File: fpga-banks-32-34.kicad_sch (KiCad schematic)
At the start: 9 parts, among them U4 XC7K160T-FFG676

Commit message: Clean schematic DRC
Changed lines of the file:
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@@
     (pin "T6")
   )
-  (symbol (lib_id "sodimm-ddr5-tester:GND") (at 79.375 253.365 0) (mirror y) (unit 1)
+  (symbol (lib_id "power:GND") (at 79.375 253.365 0) (mirror y) (unit 1)
     (in_bom yes) (on_board yes) (fields_autoplaced)
     (property "Reference" "#PWR0280" (id 0) (at 79.375 259.715 0)
       (effects (font (size 1.27 1.27)) hide)
     )
-    (property "Value" "GND" (id 1) (at 79.375 257.81 0))
-    (property "Footprint" "" (id 2) (at 79.375 253.365 0)
-      (effects (font (size 1.27 1.27)) hide)
-    )
-    (property "Datasheet" "" (id 3) (at 79.375 253.365 0)
-      (effects (font (size 1.27 1.27)) hide)
+    (property "Value" "GND" (id 1) (at 70.485 258.445 0)
+      (effects (font (size 1.27 1.27) (thickness 0.15)) (justify left bottom))
+    )
+    (property "Footprint" "" (id 2) (at 70.485 260.985 0)
+      (effects (font (size 1.27 1.27) (thickness 0.15)) (justify left bottom) hide)
+    )
+    (property "Datasheet" "" (id 3) (at 70.485 266.065 0)
+      (effects (font (size 1.27 1.27) (thickness 0.15)) (justify left bottom) hide)
     )
     (property "Author" "Antmicro" (id 4) (at 70.485 260.985 0)
@@
     (pin "1")
   )
-  (symbol (lib_id "sodimm-ddr5-tester:GND") (at 72.39 253.365 0) (mirror y) (unit 1)
+  (symbol (lib_id "power:GND") (at 72.39 253.365 0) (mirror y) (unit 1)
     (in_bom yes) (on_board yes) (fields_autoplaced)
     (property "Reference" "#PWR0279" (id 0) (at 72.39 259.715 0)
       (effects (font (size 1.27 1.27)) hide)
     )
-    (property "Value" "GND" (id 1) (at 72.39 257.81 0))
-    (property "Footprint" "" (id 2) (at 72.39 253.365 0)
-      (effects (font (size 1.27 1.27)) hide)
-    )
-    (property "Datasheet" "" (id 3) (at 72.39 253.365 0)
-      (effects (font (size 1.27 1.27)) hide)
+    (property "Value" "GND" (id 1) (at 63.5 258.445 0)
+      (effects (font (size 1.27 1.27) (thickness 0.15)) (justify left bottom))
+    )
+    (property "Footprint" "" (id 2) (at 63.5 260.985 0)
+      (effects (font (size 1.27 1.27) (thickness 0.15)) (justify left bottom) hide)
+    )
+    (property "Datasheet" "" (id 3) (at 63.5 266.065 0)
+      (effects (font (size 1.27 1.27) (thickness 0.15)) (justify left bottom) hide)
     )
     (property "Author" "Antmicro" (id 4) (at 63.5 260.985 0)
@@
     (pin "2")
   )
-  (symbol (lib_id "sodimm-ddr5-tester:GND") (at 34.29 253.365 0) (mirror y) (unit 1)
+  (symbol (lib_id "power:GND") (at 34.29 253.365 0) (mirror y) (unit 1)
     (in_bom yes) (on_board yes) (fields_autoplaced)
     (property "Reference" "#PWR0277" (id 0) (at 34.29 259.715 0)
       (effects (font (size 1.27 1.27)) hide)
     )
-    (property "Value" "GND" (id 1) (at 34.29 257.81 0))
-    (property "Footprint" "" (id 2) (at 34.29 253.365 0)
-      (effects (font (size 1.27 1.27)) hide)
-    )
-    (property "Datasheet" "" (id 3) (at 34.29 253.365 0)
-      (effects (font (size 1.27 1.27)) hide)
+    (property "Value" "GND" (id 1) (at 25.4 258.445 0)
+      (effects (font (size 1.27 1.27) (thickness 0.15)) (justify left bottom))
+    )
+    (property "Footprint" "" (id 2) (at 25.4 260.985 0)
+      (effects (font (size 1.27 1.27) (thickness 0.15)) (justify left bottom) hide)
+    )
+    (property "Datasheet" "" (id 3) (at 25.4 266.065 0)
+      (effects (font (size 1.27 1.27) (thickness 0.15)) (justify left bottom) hide)
     )
     (property "Author" "Antmicro" (id 4) (at 25.4 260.985 0)
@@
     (pin "1")
   )
-  (symbol (lib_id "sodimm-ddr5-tester:GND") (at 140.335 255.905 0) (mirror y) (unit 1)
+  (symbol (lib_id "power:GND") (at 140.335 255.905 0) (mirror y) (unit 1)
     (in_bom yes) (on_board yes) (fields_autoplaced)
     (property "Reference" "#PWR0281" (id 0) (at 140.335 262.255 0)
       (effects (font (size 1.27 1.27)) hide)
     )
-    (property "Value" "GND" (id 1) (at 140.335 260.985 0))
-    (property "Footprint" "" (id 2) (at 140.335 255.905 0)
-      (effects (font (size 1.27 1.27)) hide)
-    )
-    (property "Datasheet" "" (id 3) (at 140.335 255.905 0)
-      (effects (font (size 1.27 1.27)) hide)
+    (property "Value" "GND" (id 1) (at 131.445 260.985 0)
+      (effects (font (size 1.27 1.27) (thickness 0.15)) (justify left bottom))
+    )
+    (property "Footprint" "" (id 2) (at 131.445 263.525 0)
+      (effects (font (size 1.27 1.27) (thickness 0.15)) (justify left bottom) hide)
+    )
+    (property "Datasheet" "" (id 3) (at 131.445 268.605 0)
+      (effects (font (size 1.27 1.27) (thickness 0.15)) (justify left bottom) hide)
     )
     (property "Author" "Antmicro" (id 4) (at 131.445 263.525 0)
@@
     (pin "1")
   )
-  (symbol (lib_id "sodimm-ddr5-tester:R_80R6_0402_EIA") (at 131.445 245.745 0) (unit 1)
+  (symbol (lib_name "R_80R6_0402_EIA_1") (lib_id "sodimm-ddr5-tester:R_80R6_0402_EIA") (at 131.445 245.745 0) (unit 1)
     (in_bom yes) (on_board yes) (fields_autoplaced)
     (property "Reference" "R133" (id 0) (at 133.985 240.03 0)
@@
     (pin "2")
   )
-  (symbol (lib_id "sodimm-ddr5-tester:+1V1") (at 142.24 243.84 0) (unit 1)
+  (symbol (lib_id "power:+1V1") (at 142.24 243.84 0) (unit 1)
     (in_bom yes) (on_board yes) (fields_autoplaced)
     (property "Reference" "#PWR0282" (id 0) (at 142.24 247.65 0)
       (effects (font (size 1.27 1.27)) hide)
     )
-    (property "Value" "+1V1" (id 1) (at 142.24 238.76 0))
+    (property "Value" "+1V1" (id 1) (at 142.24 240.284 0))
     (property "Footprint" "" (id 2) (at 142.24 243.84 0)
       (effects (font (size 1.27 1.27)) hide)
@@
     (pin "2")
   )
-  (symbol (lib_id "sodimm-ddr5-tester:+1V1") (at 34.29 236.855 0) (unit 1)
+  (symbol (lib_id "power:+1V1") (at 34.29 236.855 0) (unit 1)
     (in_bom yes) (on_board yes) (fields_autoplaced)
     (property "Reference" "#PWR0276" (id 0) (at 34.29 240.665 0)
       (effects (font (size 1.27 1.27)) hide)
     )
-    (property "Value" "+1V1" (id 1) (at 34.29 231.775 0))
+    (property "Value" "+1V1" (id 1) (at 34.29 233.299 0))
     (property "Footprint" "" (id 2) (at 34.29 236.855 0)
       (effects (font (size 1.27 1.27)) hide)
@@
     (pin "2")
   )
-  (symbol (lib_id "sodimm-ddr5-tester:+1V1") (at 85.725 58.42 0) (unit 1)
+  (symbol (lib_id "power:+1V1") (at 85.725 58.42 0) (unit 1)
     (in_bom yes) (on_board yes) (fields_autoplaced)
     (property "Reference" "#PWR0266" (id 0) (at 85.725 62.23 0)
       (effects (font (size 1.27 1.27)) hide)
     )
-    (property "Value" "+1V1" (id 1) (at 85.725 54.8442 0))
+    (property "Value" "+1V1" (id 1) (at 85.725 54.864 0))
     (property "Footprint" "" (id 2) (at 85.725 58.42 0)
       (effects (font (size 1.27 1.27)) hide)
@@
     (pin "1")
   )
-  (symbol (lib_id "sodimm-ddr5-tester:+1V1") (at 216.535 58.42 0) (unit 1)
+  (symbol (lib_id "power:+1V1") (at 216.535 58.42 0) (unit 1)
     (in_bom yes) (on_board yes) (fields_autoplaced)
     (property "Reference" "#PWR0274" (id 0) (at 216.535 62.23 0)
       (effects (font (size 1.27 1.27)) hide)
     )
-    (property "Value" "+1V1" (id 1) (at 216.535 54.8442 0))
+    (property "Value" "+1V1" (id 1) (at 216.535 54.864 0))
     (property "Footprint" "" (id 2) (at 216.535 58.42 0)
       (effects (font (size 1.27 1.27)) hide)
@@
     (pin "1")
   )
-  (symbol (lib_id "sodimm-ddr5-tester:+1V1") (at 315.595 58.42 0) (unit 1)
+  (symbol (lib_id "power:+1V1") (at 315.595 58.42 0) (unit 1)
     (in_bom yes) (on_board yes) (fields_autoplaced)
     (property "Reference" "#PWR0278" (id 0) (at 315.595 62.23 0)
       (effects (font (size 1.27 1.27)) hide)
     )
-    (property "Value" "+1V1" (id 1) (at 315.595 54.8442 0))
+    (property "Value" "+1V1" (id 1) (at 315.595 54.864 0))
     (property "Footprint" "" (id 2) (at 315.595 58.42 0)
       (effects (font (size 1.27 1.27)) hide)

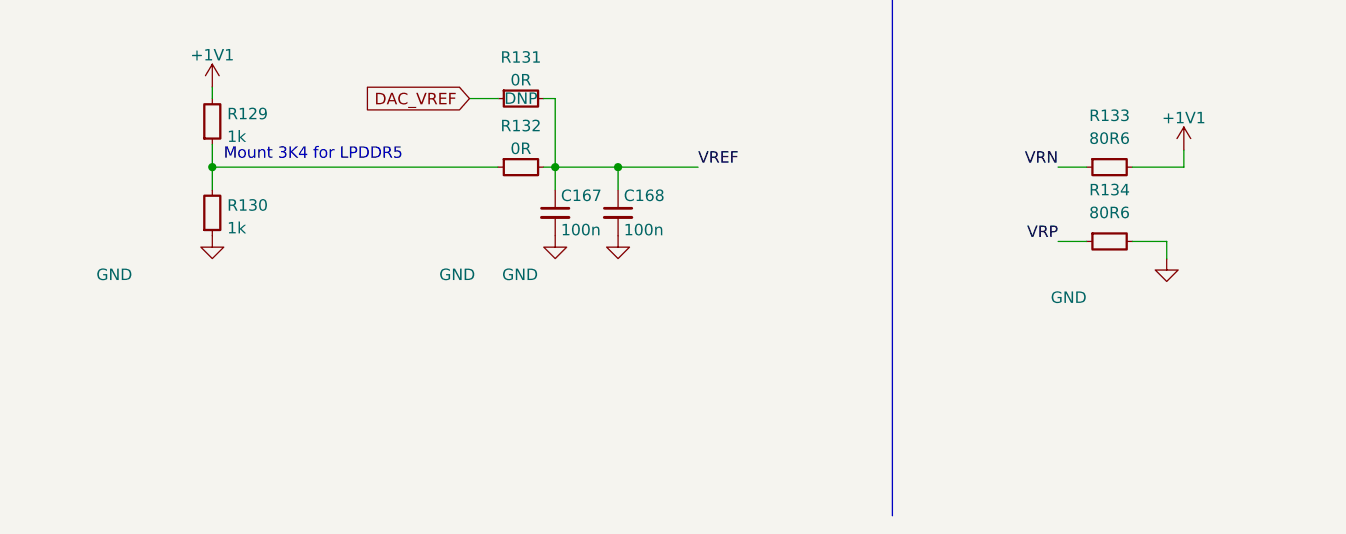
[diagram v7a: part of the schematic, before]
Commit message: Add updated components to local library
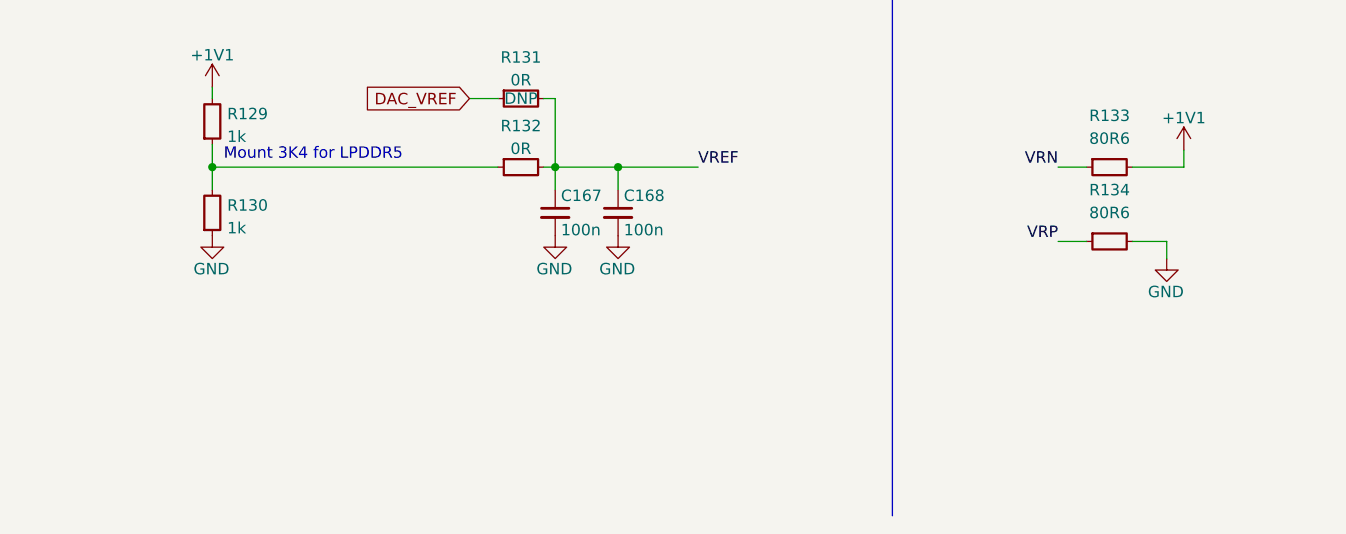
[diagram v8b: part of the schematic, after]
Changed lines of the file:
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@@
     (pin "T6")
   )
-  (symbol (lib_id "power:GND") (at 79.375 253.365 0) (mirror y) (unit 1)
+  (symbol (lib_id "sodimm-ddr5-tester:GND") (at 79.375 253.365 0) (mirror y) (unit 1)
     (in_bom yes) (on_board yes) (fields_autoplaced)
     (property "Reference" "#PWR0280" (id 0) (at 79.375 259.715 0)
       (effects (font (size 1.27 1.27)) hide)
     )
-    (property "Value" "GND" (id 1) (at 70.485 258.445 0)
+    (property "Value" "GND" (id 1) (at 81.28 257.81 0)
       (effects (font (size 1.27 1.27) (thickness 0.15)) (justify left bottom))
     )
@@
       (effects (font (size 1.27 1.27) (thickness 0.15)) (justify left bottom) hide)
     )
-    (property "Author" "Antmicro" (id 4) (at 70.485 260.985 0)
-      (effects (font (size 1.27 1.27) (thickness 0.15)) (justify left bottom) hide)
-    )
-    (property "License" "Apache-2.0" (id 5) (at 70.485 263.525 0)
+    (property "Author" "Antmicro" (id 4) (at 70.485 258.445 0)
+      (effects (font (size 1.27 1.27) (thickness 0.15)) (justify left bottom) hide)
+    )
+    (property "License" "Apache-2.0" (id 5) (at 70.485 260.985 0)
       (effects (font (size 1.27 1.27) (thickness 0.15)) (justify left bottom) hide)
     )
     (pin "1")
   )
-  (symbol (lib_id "power:GND") (at 72.39 253.365 0) (mirror y) (unit 1)
+  (symbol (lib_id "sodimm-ddr5-tester:GND") (at 72.39 253.365 0) (mirror y) (unit 1)
     (in_bom yes) (on_board yes) (fields_autoplaced)
     (property "Reference" "#PWR0279" (id 0) (at 72.39 259.715 0)
       (effects (font (size 1.27 1.27)) hide)
     )
-    (property "Value" "GND" (id 1) (at 63.5 258.445 0)
+    (property "Value" "GND" (id 1) (at 74.295 257.81 0)
       (effects (font (size 1.27 1.27) (thickness 0.15)) (justify left bottom))
     )
@@
       (effects (font (size 1.27 1.27) (thickness 0.15)) (justify left bottom) hide)
     )
-    (property "Author" "Antmicro" (id 4) (at 63.5 260.985 0)
-      (effects (font (size 1.27 1.27) (thickness 0.15)) (justify left bottom) hide)
-    )
-    (property "License" "Apache-2.0" (id 5) (at 63.5 263.525 0)
+    (property "Author" "Antmicro" (id 4) (at 63.5 258.445 0)
+      (effects (font (size 1.27 1.27) (thickness 0.15)) (justify left bottom) hide)
+    )
+    (property "License" "Apache-2.0" (id 5) (at 63.5 260.985 0)
       (effects (font (size 1.27 1.27) (thickness 0.15)) (justify left bottom) hide)
     )
@@
     (pin "2")
   )
-  (symbol (lib_id "power:GND") (at 34.29 253.365 0) (mirror y) (unit 1)
+  (symbol (lib_id "sodimm-ddr5-tester:GND") (at 34.29 253.365 0) (mirror y) (unit 1)
     (in_bom yes) (on_board yes) (fields_autoplaced)
     (property "Reference" "#PWR0277" (id 0) (at 34.29 259.715 0)
       (effects (font (size 1.27 1.27)) hide)
     )
-    (property "Value" "GND" (id 1) (at 25.4 258.445 0)
+    (property "Value" "GND" (id 1) (at 36.195 257.81 0)
       (effects (font (size 1.27 1.27) (thickness 0.15)) (justify left bottom))
     )
@@
       (effects (font (size 1.27 1.27) (thickness 0.15)) (justify left bottom) hide)
     )
-    (property "Author" "Antmicro" (id 4) (at 25.4 260.985 0)
-      (effects (font (size 1.27 1.27) (thickness 0.15)) (justify left bottom) hide)
-    )
-    (property "License" "Apache-2.0" (id 5) (at 25.4 263.525 0)
+    (property "Author" "Antmicro" (id 4) (at 25.4 258.445 0)
+      (effects (font (size 1.27 1.27) (thickness 0.15)) (justify left bottom) hide)
+    )
+    (property "License" "Apache-2.0" (id 5) (at 25.4 260.985 0)
       (effects (font (size 1.27 1.27) (thickness 0.15)) (justify left bottom) hide)
     )
     (pin "1")
   )
-  (symbol (lib_id "power:GND") (at 140.335 255.905 0) (mirror y) (unit 1)
+  (symbol (lib_id "sodimm-ddr5-tester:GND") (at 140.335 255.905 0) (mirror y) (unit 1)
     (in_bom yes) (on_board yes) (fields_autoplaced)
     (property "Reference" "#PWR0281" (id 0) (at 140.335 262.255 0)
       (effects (font (size 1.27 1.27)) hide)
     )
-    (property "Value" "GND" (id 1) (at 131.445 260.985 0)
+    (property "Value" "GND" (id 1) (at 142.24 260.35 0)
       (effects (font (size 1.27 1.27) (thickness 0.15)) (justify left bottom))
     )
@@
       (effects (font (size 1.27 1.27) (thickness 0.15)) (justify left bottom) hide)
     )
-    (property "Author" "Antmicro" (id 4) (at 131.445 263.525 0)
-      (effects (font (size 1.27 1.27) (thickness 0.15)) (justify left bottom) hide)
-    )
-    (property "License" "Apache-2.0" (id 5) (at 131.445 266.065 0)
+    (property "Author" "Antmicro" (id 4) (at 131.445 260.985 0)
+      (effects (font (size 1.27 1.27) (thickness 0.15)) (justify left bottom) hide)
+    )
+    (property "License" "Apache-2.0" (id 5) (at 131.445 263.525 0)
       (effects (font (size 1.27 1.27) (thickness 0.15)) (justify left bottom) hide)
     )
     (pin "1")
   )
-  (symbol (lib_name "R_80R6_0402_EIA_1") (lib_id "sodimm-ddr5-tester:R_80R6_0402_EIA") (at 131.445 245.745 0) (unit 1)
+  (symbol (lib_id "sodimm-ddr5-tester:R_80R6_0402_EIA") (at 131.445 245.745 0) (unit 1)
     (in_bom yes) (on_board yes) (fields_autoplaced)
     (property "Reference" "R133" (id 0) (at 133.985 240.03 0)
@@
     (pin "2")
   )
-  (symbol (lib_id "power:+1V1") (at 142.24 243.84 0) (unit 1)
+  (symbol (lib_id "sodimm-ddr5-tester:+1V1") (at 142.24 243.84 0) (unit 1)
     (in_bom yes) (on_board yes) (fields_autoplaced)
     (property "Reference" "#PWR0282" (id 0) (at 142.24 247.65 0)
@@
     (pin "2")
   )
-  (symbol (lib_id "power:+1V1") (at 34.29 236.855 0) (unit 1)
+  (symbol (lib_id "sodimm-ddr5-tester:+1V1") (at 34.29 236.855 0) (unit 1)
     (in_bom yes) (on_board yes) (fields_autoplaced)
     (property "Reference" "#PWR0276" (id 0) (at 34.29 240.665 0)
@@
     (pin "2")
   )
-  (symbol (lib_id "power:+1V1") (at 85.725 58.42 0) (unit 1)
+  (symbol (lib_id "sodimm-ddr5-tester:+1V1") (at 85.725 58.42 0) (unit 1)
     (in_bom yes) (on_board yes) (fields_autoplaced)
     (property "Reference" "#PWR0266" (id 0) (at 85.725 62.23 0)
@@
     (pin "1")
   )
-  (symbol (lib_id "power:+1V1") (at 216.535 58.42 0) (unit 1)
+  (symbol (lib_id "sodimm-ddr5-tester:+1V1") (at 216.535 58.42 0) (unit 1)
     (in_bom yes) (on_board yes) (fields_autoplaced)
     (property "Reference" "#PWR0274" (id 0) (at 216.535 62.23 0)
@@
     (pin "1")
   )
-  (symbol (lib_id "power:+1V1") (at 315.595 58.42 0) (unit 1)
+  (symbol (lib_id "sodimm-ddr5-tester:+1V1") (at 315.595 58.42 0) (unit 1)
     (in_bom yes) (on_board yes) (fields_autoplaced)
     (property "Reference" "#PWR0278" (id 0) (at 315.595 62.23 0)
